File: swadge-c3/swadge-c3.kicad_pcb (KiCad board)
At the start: 2 copper layers, 73.7 x 89.4 mm, 68 parts, among them J1 USB_B_Micro, SW1 4-1437565-2, SW2 4-1437565-2, SW3 4-1437565-2, SW4 4-1437565-2, SW5 4-1437565-2, SW6 4-1437565-2, SW7 4-1437565-2, SW8 4-1437565-2, SW9 SW_SPDT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

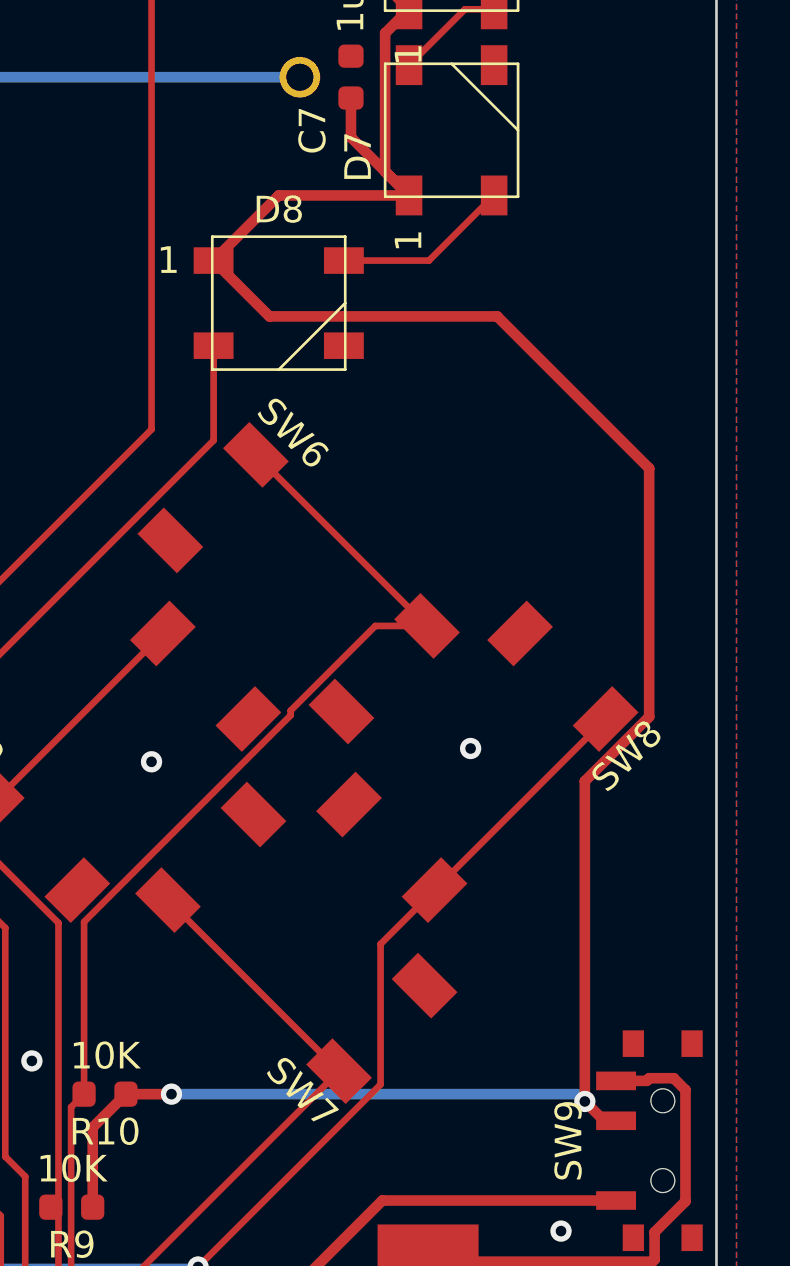
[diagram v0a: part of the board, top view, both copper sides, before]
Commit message: Added three way thumbswitch
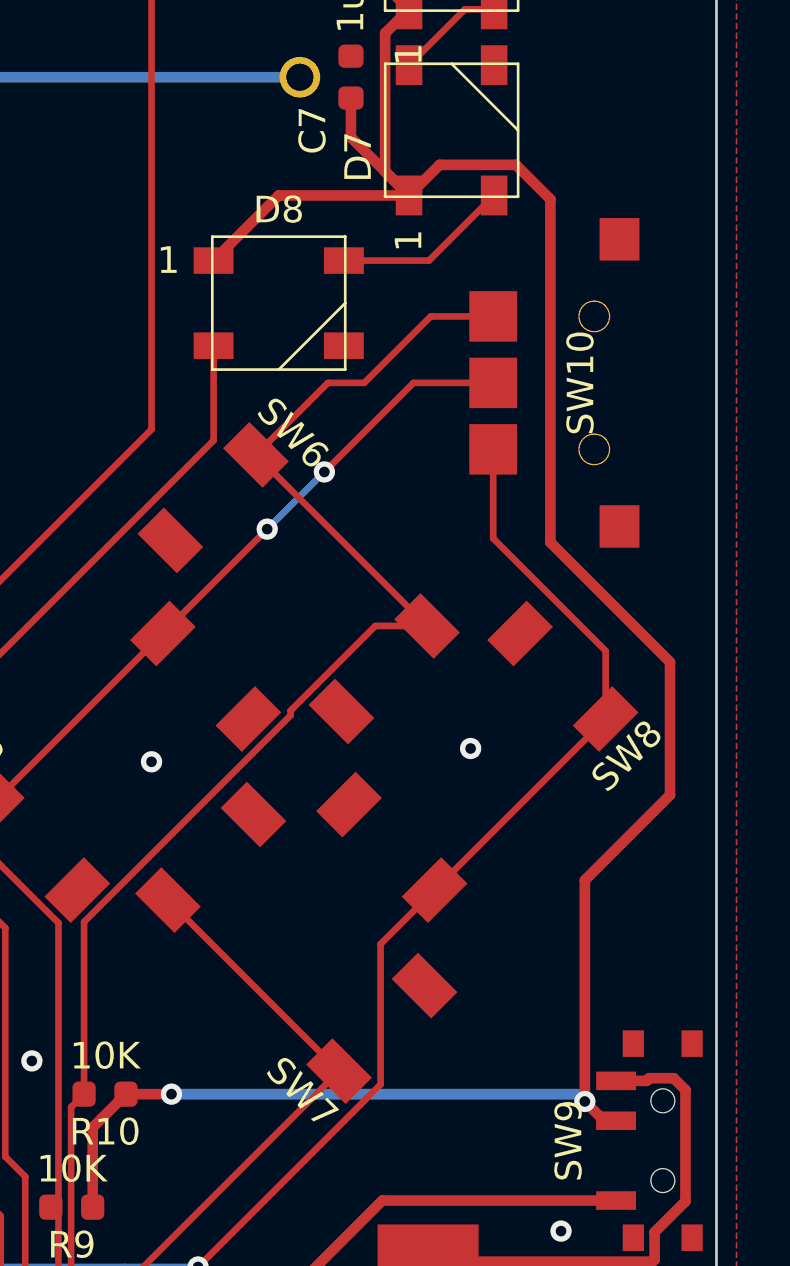
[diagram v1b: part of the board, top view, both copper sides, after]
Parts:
- added SW10: LEVER8184, Swadge_Parts:LEVER8184, F.Cu at (177.7, 94.0)
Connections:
- J1 pad 2: (no net) -> Net-(J1-Pad2)
- J1 pad 3: (no net) -> Net-(J1-Pad3)
- J1 pad 4: (no net) -> Net-(J1-Pad4)
- U3 pad 10: (no net) -> Net-(U3-Pad10)
- U3 pad 15: (no net) -> Net-(U3-Pad15)
- U3 pad 17: (no net) -> Net-(U3-Pad17)
- U3 pad 24: (no net) -> Net-(U3-Pad24)
- U3 pad 25: (no net) -> Net-(U3-Pad25)
- U3 pad 28: (no net) -> Net-(U3-Pad28)
- U3 pad 29: (no net) -> Net-(U3-Pad29)
- U3 pad 32: (no net) -> Net-(U3-Pad32)
- U3 pad 33: (no net) -> Net-(U3-Pad33)
- U3 pad 34: (no net) -> Net-(U3-Pad34)
- U3 pad 35: (no net) -> Net-(U3-Pad35)
- U3 pad 4: (no net) -> Net-(U3-Pad4)
- U3 pad 7: (no net) -> Net-(U3-Pad7)
- U3 pad 9: (no net) -> Net-(U3-Pad9)
- U5 pad 7: (no net) -> Net-(U5-Pad7)
- U7 pad 11: (no net) -> Net-(U7-Pad11)
- U7 pad 5: (no net) -> Net-(U7-Pad5)
- U7 pad 6: (no net) -> Net-(U7-Pad6)
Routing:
- net IO8_SW5: track 66.1 -> 82.4 mm, vias 4 -> 6
- net IO19_SW8: track 59.6 -> 71.4 mm
- net IO9_SW6: track 78.4 -> 89.5 mm
- net +3V3: track 361.2 -> 360.2 mm

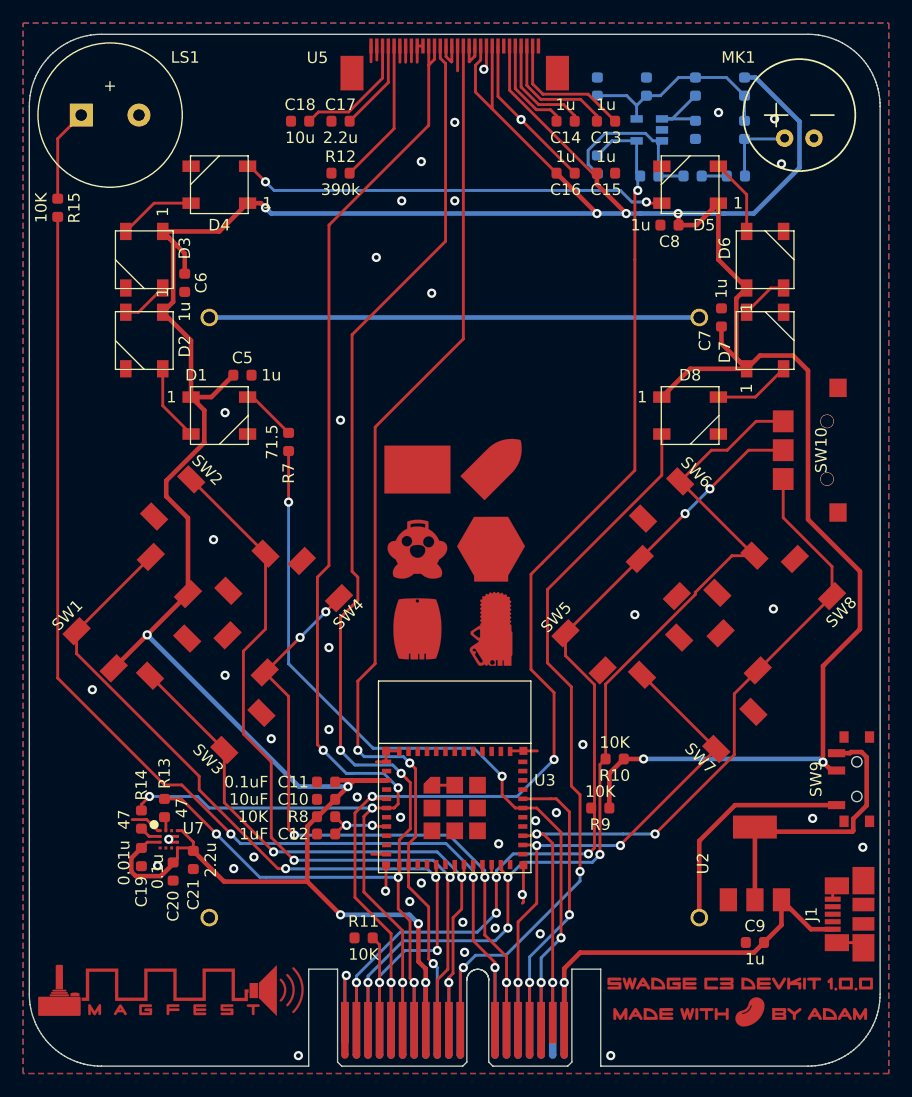
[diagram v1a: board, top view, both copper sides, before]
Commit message: Replaced four left buttons with scrollwheel
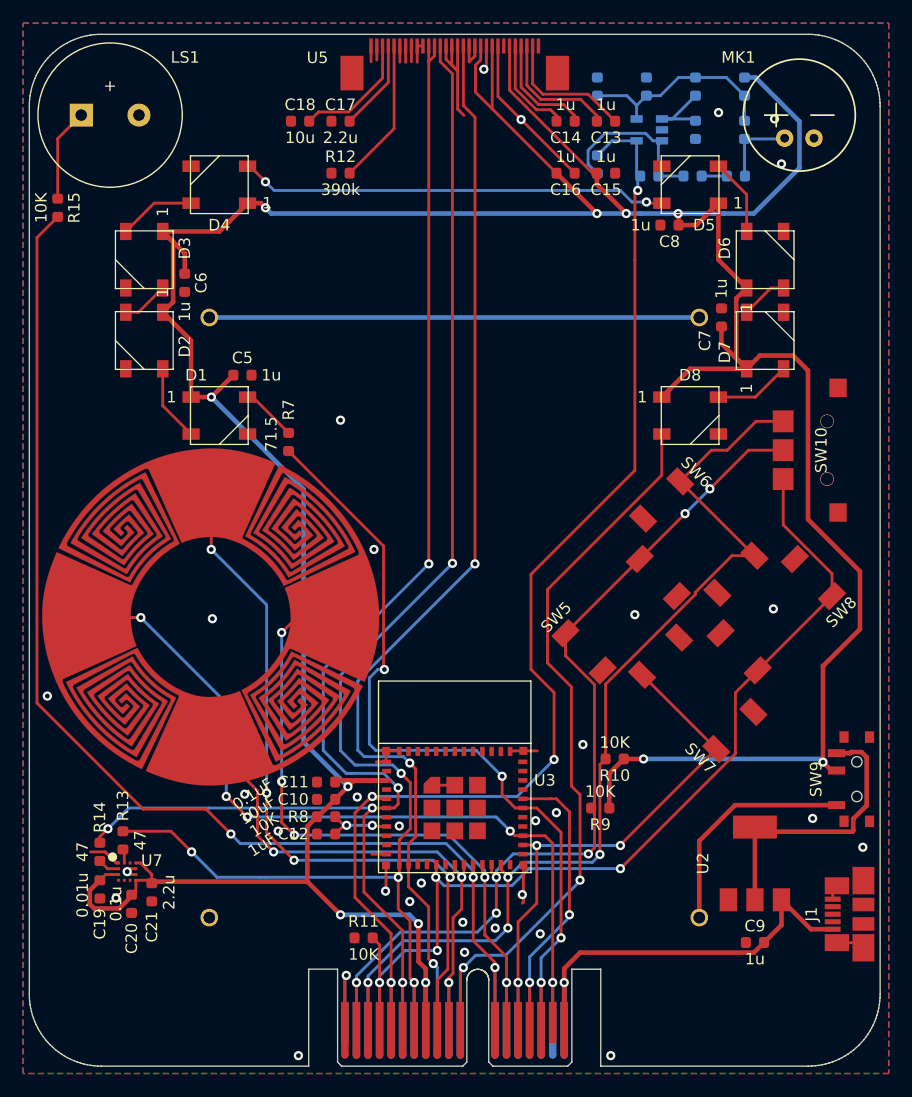
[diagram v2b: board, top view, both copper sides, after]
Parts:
- removed Ref**: Val**, swadge-c3-art:swadges
- removed Ref**: Val**, swadge-c3-art:label
- removed Ref**: Val**, swadge-c3-art:mag-logo-metal
- removed SW1, SW2, SW3, SW4: 4-1437565-2, Swadge_Parts:SW_4-1437565-2
- added SW11: Val**, Swadge_Parts:scroll-4, F.Cu at (124.2, 108.5)
- moved U7 4.56 mm to (117.0, 130.5)
- moved C19 4.56 mm to (114.7, 132.1)
- moved C20 4.56 mm to (117.4, 133.3)
- moved C21 4.56 mm to (119.2, 132.3)
- moved R14 4.56 mm to (114.7, 128.8)
- moved R13 4.56 mm to (116.7, 127.8)
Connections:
- net IO4_SW2 renamed IO4_SCU
- net IO5_SW3 renamed IO5_SCD
- net IO7_SW4 renamed IO7_SCR
- J1 pad 2: Net-(J1-Pad2) -> (no net)
- J1 pad 3: Net-(J1-Pad3) -> (no net)
- J1 pad 4: Net-(J1-Pad4) -> (no net)
- R11 pad 2: IO10_SW1 -> IO10_SW8
- SW10 pad 2: IO19_SW8 -> IO10_SW8
- SW8 pad 1: IO19_SW8 -> IO10_SW8
- SW8 pad 2: IO19_SW8 -> IO10_SW8
- U3 pad 10: Net-(U3-Pad10) -> (no net)
- U3 pad 15: Net-(U3-Pad15) -> (no net)
- U3 pad 16: IO10_SW1 -> IO10_SW8
- U3 pad 17: Net-(U3-Pad17) -> (no net)
- U3 pad 24: Net-(U3-Pad24) -> (no net)
- U3 pad 25: Net-(U3-Pad25) -> (no net)
- U3 pad 27: IO19_SW8 -> IO19_SCL
- U3 pad 28: Net-(U3-Pad28) -> (no net)
- U3 pad 29: Net-(U3-Pad29) -> (no net)
- U3 pad 32: Net-(U3-Pad32) -> (no net)
- U3 pad 33: Net-(U3-Pad33) -> (no net)
- U3 pad 34: Net-(U3-Pad34) -> (no net)
- U3 pad 35: Net-(U3-Pad35) -> (no net)
- U3 pad 4: Net-(U3-Pad4) -> (no net)
- U3 pad 7: Net-(U3-Pad7) -> (no net)
- U3 pad 9: Net-(U3-Pad9) -> (no net)
- U4 pad A17: IO19_SW8 -> IO19_SCL
- U4 pad A4: IO10_SW1 -> IO10_SW8
- U4 pad B17: IO19_SW8 -> IO19_SCL
- U4 pad B4: IO10_SW1 -> IO10_SW8
- U5 pad 7: Net-(U5-Pad7) -> (no net)
- U7 pad 11: Net-(U7-Pad11) -> (no net)
- U7 pad 5: Net-(U7-Pad5) -> (no net)
- U7 pad 6: Net-(U7-Pad6) -> (no net)
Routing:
- net IO10_SW8: track 0.00 -> 85.9 mm, vias 0 -> 4
- net IO10_SW1: track 76.8 -> 0.00 mm, vias 4 -> 0
- net IO19_SCL: track 0.00 -> 72.9 mm, vias 0 -> 5
- net IO19_SW8: track 71.4 -> 0.00 mm, vias 3 -> 0
- net +3V3: track 360.2 -> 349.8 mm
- net IO5_SCD: track 55.5 -> 47.4 mm
- net GND: track 64.0 -> 70.0 mm, vias 44 -> 33
- net IO6_BZR: track 103.5 -> 107.3 mm
- net IO3_SDA: track 124.5 -> 127.8 mm
- net IO4_SCU: track 67.2 -> 64.0 mm, vias 2 -> 4
- net IO0_SCL: track 121.8 -> 124.4 mm
- net RX: track 70.6 -> 72.0 mm
- net IO7_SCR: track 61.5 -> 60.6 mm
- net IO1_RES: track 94.2 -> 95.1 mm

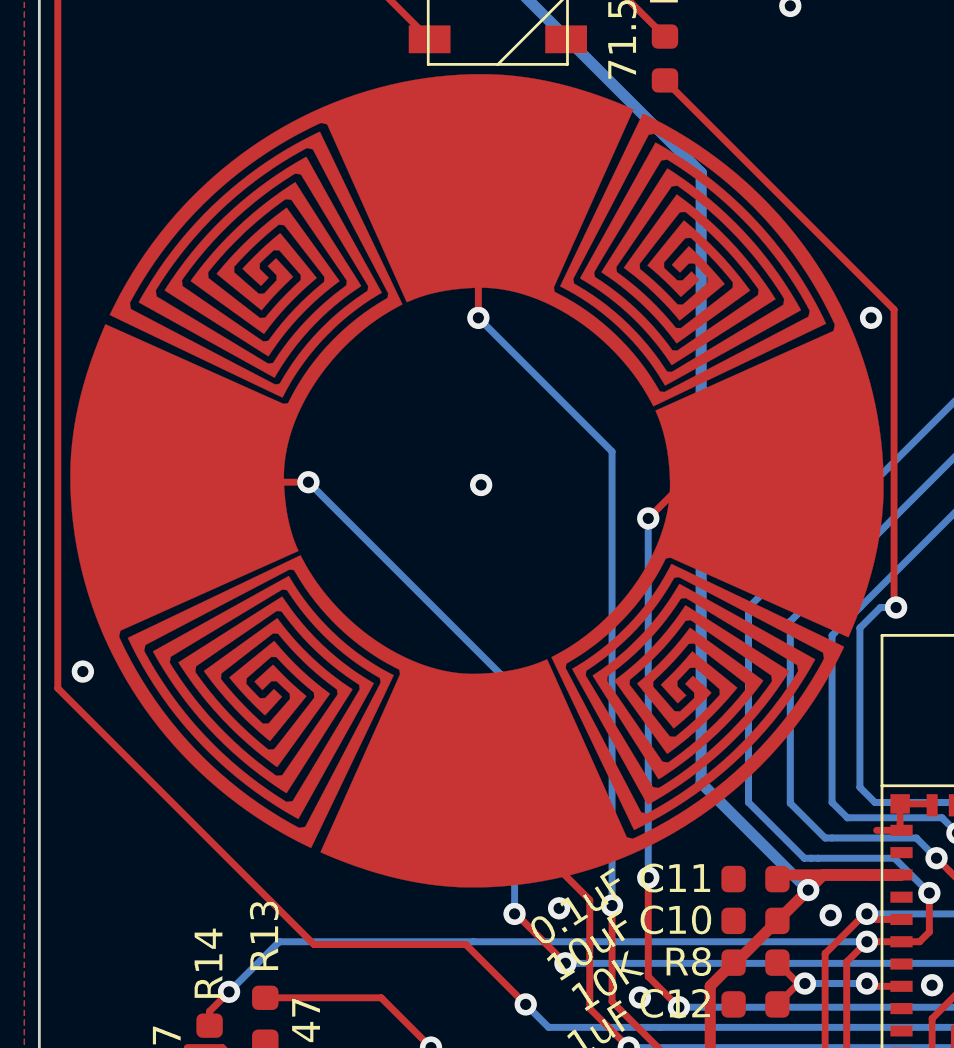
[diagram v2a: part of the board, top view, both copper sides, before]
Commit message: Added pullups
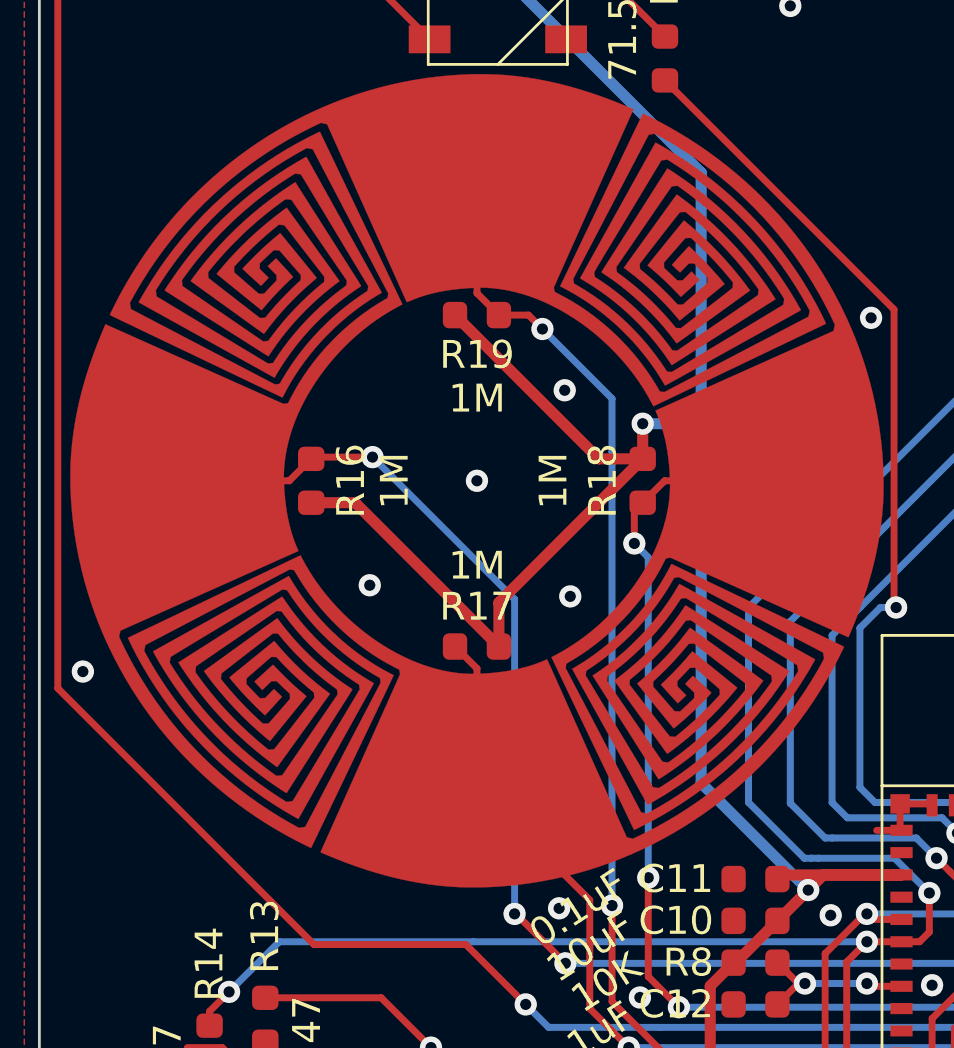
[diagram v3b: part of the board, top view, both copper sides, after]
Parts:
- added R16: 1M, Swadge_Parts:R_0603_1608Metric, F.Cu at (118.3, 108.5)
- added R17: 1M, Swadge_Parts:R_0603_1608Metric, F.Cu at (124.2, 114.4)
- added R18: 1M, Swadge_Parts:R_0603_1608Metric, F.Cu at (130.2, 108.5)
- added R19: 1M, Swadge_Parts:R_0603_1608Metric, F.Cu at (124.2, 102.5)
- SW11: value Val** -> scroll-4
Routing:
- net +3V3: track 349.8 -> 379.8 mm, vias 11 -> 12
- net IO5_SCD: track 47.4 -> 52.8 mm
- net IO19_SCL: track 72.9 -> 75.4 mm
- net IO7_SCR: track 60.6 -> 61.5 mm
- net IO4_SCU: track 64.0 -> 64.7 mm
- net GND: vias 33 -> 36
